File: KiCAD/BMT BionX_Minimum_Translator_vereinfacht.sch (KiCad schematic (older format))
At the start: 35 parts, among them J1 Kunteng Display Connector, J2 SAE Power Connector Motor, J3 Rosenberg Motor, J4 External BB Torquesensor, J5 Brake connector, J6 Throttle connector, J7 CAN Connector, J9 Batterieanschluß, Q1 IRF3205, Q2 IRF3205, Q3 BCP56, U1 BP, U2 MCP2551-CAN Transceiver, U3 VOM1271, U4 SD12-5, U5 VOM1271

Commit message: Schematic as PDF
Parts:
- added C7, C8, C9: 10µ, Capacitor_THT:CP_Radial_D5.0mm_P2.50mm, symbol Device:CP
- added U6: LM7812_TO220, Package_TO_SOT_THT:TO-220-3_Vertical, symbol Regulator_Linear:LM7812_TO220
- added U7: LM7805_TO220, Package_TO_SOT_THT:TO-220-3_Vertical, symbol Regulator_Linear:LM7805_TO220
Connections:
- net GND: now also C7.2, C8.2, C9.2, U6.2 (GND), U7.2 (GND)
- net at J3.1 (Pin_1), J4.1 (Pin_1), U4.+12V: now also C8.1, U6.3 (VO), U7.1 (VI)
- net at J5.1 (Pin_1), J6.1 (Pin_1), U1.5V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: now also C9.1, U7.3 (VO)
- net at R12.2, U4.V_in: now also C7.1, U6.1 (VI)
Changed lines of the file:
@@
 $EndComp
 Wire Wire Line
-	5650 2450 5650 2550
+	5650 2450 5650 2500
 $Comp
 L Device:R R11
@@
 Wire Wire Line
 	4950 2750 4950 2550
+$Comp
+L Regulator_Linear:LM7812_TO220 U6
+U 1 1 5F87B01F
+P 2450 4950
+F 0 "U6" H 2450 5192 50  0000 C CNN
+F 1 "LM7812_TO220" H 2450 5101 50  0000 C CNN
+F 2 "Package_TO_SOT_THT:TO-220-3_Vertical" H 2450 5175 50  0001 C CIN
+F 3 "http://www.fairchildsemi.com/ds/LM/LM7805.pdf" H 2450 4900 50  0001 C CNN
+	1    2450 4950
+	1    0    0    -1
+$EndComp
+$Comp
+L Regulator_Linear:LM7805_TO220 U7
+U 1 1 5F87C4AD
+P 2450 5650
+F 0 "U7" H 2450 5892 50  0000 C CNN
+F 1 "LM7805_TO220" H 2450 5801 50  0000 C CNN
+F 2 "Package_TO_SOT_THT:TO-220-3_Vertical" H 2450 5875 50  0001 C CIN
+F 3 "http://www.fairchildsemi.com/ds/LM/LM7805.pdf" H 2450 5600 50  0001 C CNN
+	1    2450 5650
+	1    0    0    -1
+$EndComp
+$Comp
+L Device:CP C8
+U 1 1 5F87D97A
+P 3000 5050
+F 0 "C8" H 3118 5096 50  0000 L CNN
+F 1 "10µ" H 3118 5005 50  0000 L CNN
+F 2 "Capacitor_THT:CP_Radial_D5.0mm_P2.50mm" H 3038 4900 50  0001 C CNN
+F 3 "~" H 3000 5050 50  0001 C CNN
+	1    3000 5050
+	1    0    0    -1
+$EndComp
+$Comp
+L Device:CP C7
+U 1 1 5F87E84B
+P 1700 5050
+F 0 "C7" H 1818 5096 50  0000 L CNN
+F 1 "10µ" H 1818 5005 50  0000 L CNN
+F 2 "Capacitor_THT:CP_Radial_D5.0mm_P2.50mm" H 1738 4900 50  0001 C CNN
+F 3 "~" H 1700 5050 50  0001 C CNN
+	1    1700 5050
+	1    0    0    -1
+$EndComp
+$Comp
+L Device:CP C9
+U 1 1 5F87F419
+P 3050 5700
+F 0 "C9" H 3168 5746 50  0000 L CNN
+F 1 "10µ" H 3168 5655 50  0000 L CNN
+F 2 "Capacitor_THT:CP_Radial_D5.0mm_P2.50mm" H 3088 5550 50  0001 C CNN
+F 3 "~" H 3050 5700 50  0001 C CNN
+	1    3050 5700
+	1    0    0    -1
+$EndComp
+Wire Wire Line
+	1300 4350 1300 5250
+Wire Wire Line
+	1300 5250 1700 5250
+Connection ~ 1300 4350
+Wire Wire Line
+	2450 5250 3000 5250
+Wire Wire Line
+	3000 5250 3000 5200
+Connection ~ 2450 5250
+Wire Wire Line
+	1700 5250 1700 5200
+Connection ~ 1700 5250
+Wire Wire Line
+	1700 5250 2450 5250
+Wire Wire Line
+	1300 5250 1300 5950
+Wire Wire Line
+	1300 5950 2450 5950
+Connection ~ 1300 5250
+Wire Wire Line
+	2450 5950 3050 5950
+Wire Wire Line
+	3050 5850 3050 5950
+Connection ~ 2450 5950
+Wire Wire Line
+	4900 4300 4150 4300
+Wire Wire Line
+	4150 4300 4150 5450
+Wire Wire Line
+	4150 5450 3050 5450
+Wire Wire Line
+	2750 5450 2750 5650
+Connection ~ 4900 4300
+Wire Wire Line
+	3050 5450 3050 5550
+Connection ~ 3050 5450
+Wire Wire Line
+	3050 5450 2750 5450
+Wire Wire Line
+	5500 4100 3850 4100
+Wire Wire Line
+	3850 4100 3850 4900
+Wire Wire Line
+	3850 4900 3450 4900
+Connection ~ 5500 4100
+Wire Wire Line
+	2750 4900 2750 4950
+Wire Wire Line
+	3000 4900 2750 4900
+Connection ~ 3000 4900
+Wire Wire Line
+	5650 2500 5350 2500
+Wire Wire Line
+	5350 2500 5350 2750
+Wire Wire Line
+	5350 2750 5050 2750
+Wire Wire Line
+	5050 2750 5050 3850
+Wire Wire Line
+	5050 3850 3450 3850
+Wire Wire Line
+	3450 3850 3450 4600
+Wire Wire Line
+	3450 4600 2050 4600
+Wire Wire Line
+	2050 4600 2050 4900
+Wire Wire Line
+	2050 4950 2150 4950
+Connection ~ 5650 2500
+Wire Wire Line
+	5650 2500 5650 2550
+Wire Wire Line
+	2050 4900 1700 4900
+Connection ~ 2050 4900
+Wire Wire Line
+	2050 4900 2050 4950
+Wire Wire Line
+	3450 4900 3450 5350
+Wire Wire Line
+	3450 5350 2000 5350
+Wire Wire Line
+	2000 5350 2000 5650
+Wire Wire Line
+	2000 5650 2150 5650
+Connection ~ 3450 4900
+Wire Wire Line
+	3450 4900 3000 4900
 $EndSCHEMATC

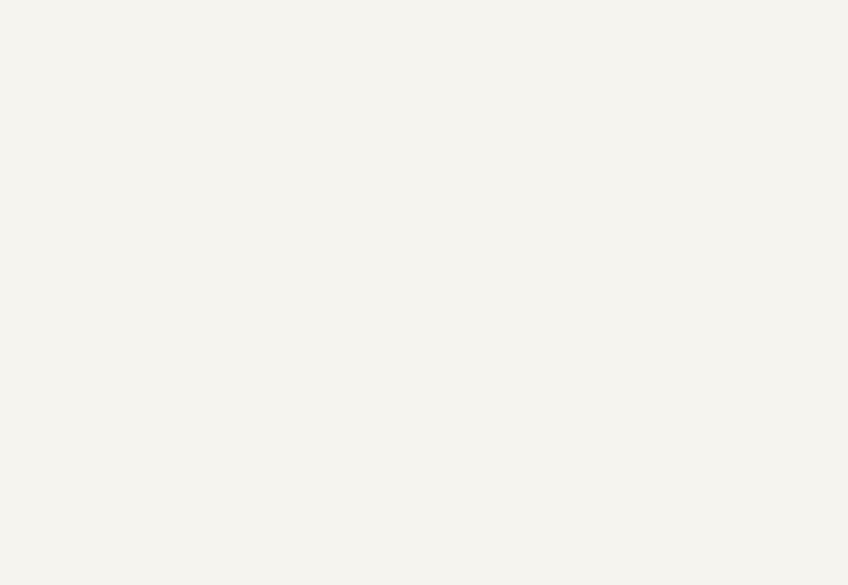
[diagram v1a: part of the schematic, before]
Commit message: added filter for speedsignal
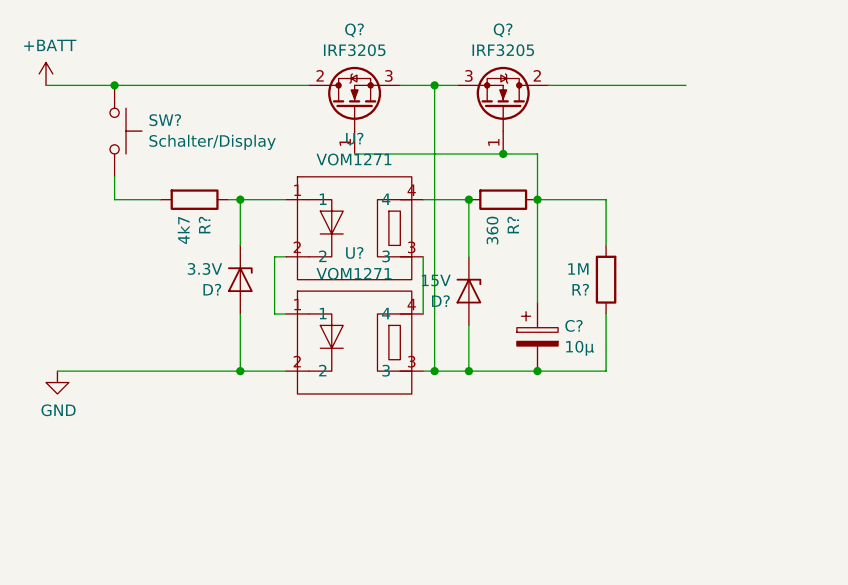
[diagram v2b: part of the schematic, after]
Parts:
- added C?: 10µ, Capacitor_THT:CP_Radial_D5.0mm_P2.50mm, symbol Device:CP
- added D?: 15V, Diode_SMD:D_0805_2012Metric, symbol Device:D_Zener
- added D?: 3.3V, Diode_SMD:D_0805_2012Metric, symbol Device:D_Zener
- added Q? (x2): IRF3205, Package_TO_SOT_THT:TO-220-3_Vertical, symbol Transistor_FET:IRF3205
- added R?: 360, Resistor_SMD:R_0805_2012Metric, symbol Device:R
- added R?: 4k7, Resistor_SMD:R_0805_2012Metric, symbol Device:R
- added R?: 1M, Resistor_SMD:R_0805_2012Metric, symbol Device:R
- added SW?: Schalter/Display, symbol Switch:SW_Push
- added U? (x2): VOM1271, Package_SO:SOP-4_3.8x4.1mm_P2.54mm, symbol Driver_FET:VOM1271
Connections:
- net +BATT: now also Q?.2 (D), SW?.1
- net GND: now also D?.2 (A), U?.2
- new net: C?.1, Q?.1 (G), Q?.1 (G), R?.1, R?.2
- new net: C?.2, D?.2 (A), Q?.3 (S), Q?.3 (S), R?.1, U?.3
- new net: D?.1 (K), R?.1, U?.1
- new net: U?.1, U?.2
- new net: U?.3, U?.4
- new net: D?.1 (K), R?.2, U?.4
- new net: R?.2, SW?.2
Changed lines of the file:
@@
 Wire Wire Line
 	3450 4900 3000 4900
+$Comp
+L Transistor_FET:IRF3205 Q?
+U 1 1 5FA7240E
+P -2000 750
+F 0 "Q?" V -1657 750 50  0000 C CNN
+F 1 "IRF3205" V -1748 750 50  0000 C CNN
+F 2 "Package_TO_SOT_THT:TO-220-3_Vertical" H -1750 675 50  0001 L CIN
+F 3 "http://www.irf.com/product-info/datasheets/data/irf3205.pdf" H -2000 750 50  0001 L CNN
+	1    -2000 750
+	0    -1   -1   0
+$EndComp
+$Comp
+L Transistor_FET:IRF3205 Q?
+U 1 1 5FA72414
+P -1350 750
+F 0 "Q?" V -1007 750 50  0000 C CNN
+F 1 "IRF3205" V -1098 750 50  0000 C CNN
+F 2 "Package_TO_SOT_THT:TO-220-3_Vertical" H -1100 675 50  0001 L CIN
+F 3 "http://www.irf.com/product-info/datasheets/data/irf3205.pdf" H -1350 750 50  0001 L CNN
+	1    -1350 750
+	0    1    -1   0
+$EndComp
+$Comp
+L Driver_FET:VOM1271 U?
+U 1 1 5FA7241A
+P -2000 900
+F 0 "U?" H -2000 915 50  0000 C CNN
+F 1 "VOM1271" H -2000 824 50  0000 C CNN
+F 2 "Package_SO:SOP-4_3.8x4.1mm_P2.54mm" H -2000 900 50  0001 C CNN
+F 3 "" H -2000 900 50  0001 C CNN
+	1    -2000 900
+	1    0    0    -1
+$EndComp
+$Comp
+L Driver_FET:VOM1271 U?
+U 1 1 5FA72420
+P -2000 1400
+F 0 "U?" H -2000 1415 50  0000 C CNN
+F 1 "VOM1271" H -2000 1324 50  0000 C CNN
+F 2 "Package_SO:SOP-4_3.8x4.1mm_P2.54mm" H -2000 1400 50  0001 C CNN
+F 3 "" H -2000 1400 50  0001 C CNN
+	1    -2000 1400
+	1    0    0    -1
+$EndComp
+Wire Wire Line
+	-2350 1650 -2300 1650
+Wire Wire Line
+	-1700 1650 -1700 1400
+Wire Wire Line
+	-1700 1150 -1500 1150
+Wire Wire Line
+	-1700 1900 -1650 1900
+Wire Wire Line
+	-1650 1900 -1650 650
+Connection ~ -1650 650
+Wire Wire Line
+	-1650 650  -1550 650
+$Comp
+L Device:D_Zener D?
+U 1 1 5FA7243B
+P -1500 1550
+F 0 "D?" V -1454 1471 50  0000 R CNN
+F 1 "15V" V -1545 1471 50  0000 R CNN
+F 2 "Diode_SMD:D_0805_2012Metric" H -1500 1550 50  0001 C CNN
+F 3 "~" H -1500 1550 50  0001 C CNN
+	1    -1500 1550
+	0    1    1    0
+$EndComp
+Wire Wire Line
+	-3350 650  -3050 650
+Wire Wire Line
+	-2300 1400 -2350 1400
+Wire Wire Line
+	-2350 1400 -2350 1650
+$Comp
+L Device:R R?
+U 1 1 5FAA2E19
+P -1350 1150
+F 0 "R?" H -1280 1196 50  0000 L CNN
+F 1 "360" H -1280 1105 50  0000 L CNN
+F 2 "Resistor_SMD:R_0805_2012Metric" V -1420 1150 50  0001 C CNN
+F 3 "~" H -1350 1150 50  0001 C CNN
+	1    -1350 1150
+	0    1    1    0
+$EndComp
+Wire Wire Line
+	-1500 1150 -1500 1400
+Wire Wire Line
+	-1800 650  -1650 650
+Wire Wire Line
+	-2000 950  -1350 950
+Connection ~ -1500 1150
+Wire Wire Line
+	-1500 1700 -1500 1900
+Wire Wire Line
+	-1500 1900 -1650 1900
+Connection ~ -1650 1900
+$Comp
+L Device:CP C?
+U 1 1 5FAE6A47
+P -1200 1750
+F 0 "C?" H -1082 1796 50  0000 L CNN
+F 1 "10µ" H -1082 1705 50  0000 L CNN
+F 2 "Capacitor_THT:CP_Radial_D5.0mm_P2.50mm" H -1162 1600 50  0001 C CNN
+F 3 "~" H -1200 1750 50  0001 C CNN
+	1    -1200 1750
+	1    0    0    -1
+$EndComp
+Wire Wire Line
+	-1500 1900 -1200 1900
+Connection ~ -1500 1900
+Wire Wire Line
+	-1200 1600 -1200 1150
+Wire Wire Line
+	-1200 1150 -1200 950
+Wire Wire Line
+	-1200 950  -1350 950
+Connection ~ -1200 1150
+Connection ~ -1350 950
+$Comp
+L Device:D_Zener D?
+U 1 1 5FB2B7AF
+P -2500 1500
+F 0 "D?" V -2454 1421 50  0000 R CNN
+F 1 "3.3V" V -2545 1421 50  0000 R CNN
+F 2 "Diode_SMD:D_0805_2012Metric" H -2500 1500 50  0001 C CNN
+F 3 "~" H -2500 1500 50  0001 C CNN
+	1    -2500 1500
+	0    1    1    0
+$EndComp
+$Comp
+L Switch:SW_Push SW?
+U 1 1 5FB2D20E
+P -3050 850
+F 0 "SW?" V -3096 998 50  0000 L CNN
+F 1 "Schalter/Display" V -3005 998 50  0000 L CNN
+F 2 "" H -3050 1050 50  0001 C CNN
+F 3 "~" H -3050 1050 50  0001 C CNN
+	1    -3050 850
+	0    1    1    0
+$EndComp
+Connection ~ -3050 650
+Wire Wire Line
+	-3050 650  -2200 650
+$Comp
+L Device:R R?
+U 1 1 5FB45B50
+P -2700 1150
+F 0 "R?" H -2630 1196 50  0000 L CNN
+F 1 "4k7" H -2630 1105 50  0000 L CNN
+F 2 "Resistor_SMD:R_0805_2012Metric" V -2770 1150 50  0001 C CNN
+F 3 "~" H -2700 1150 50  0001 C CNN
+	1    -2700 1150
+	0    1    1    0
+$EndComp
+Wire Wire Line
+	-3050 1050 -3050 1150
+Wire Wire Line
+	-3050 1150 -2850 1150
+Wire Wire Line
+	-2550 1150 -2500 1150
+Wire Wire Line
+	-2500 1150 -2500 1350
+Connection ~ -2500 1150
+Wire Wire Line
+	-2500 1150 -2300 1150
+Wire Wire Line
+	-2500 1650 -2500 1900
+Wire Wire Line
+	-2500 1900 -2300 1900
+$Comp
+L power:+BATT #PWR?
+U 1 1 5FBA561B
+P -3350 650
+F 0 "#PWR?" H -3350 500 50  0001 C CNN
+F 1 "+BATT" H -3335 823 50  0000 C CNN
+F 2 "" H -3350 650 50  0001 C CNN
+F 3 "" H -3350 650 50  0001 C CNN
+	1    -3350 650
+	1    0    0    -1
+$EndComp
+$Comp
+L power:GND #PWR?
+U 1 1 5FBA62CD
+P -3300 1900
+F 0 "#PWR?" H -3300 1650 50  0001 C CNN
+F 1 "GND" H -3295 1727 50  0000 C CNN
+F 2 "" H -3300 1900 50  0001 C CNN
+F 3 "" H -3300 1900 50  0001 C CNN
+	1    -3300 1900
+	1    0    0    -1
+$EndComp
+Wire Wire Line
+	-3300 1900 -2500 1900
+Connection ~ -2500 1900
+Wire Wire Line
+	-1150 650  -550 650
+$Comp
+L Device:R R?
+U 1 1 5FBD75F6
+P -900 1500
+F 0 "R?" H -830 1546 50  0000 L CNN
+F 1 "1M" H -830 1455 50  0000 L CNN
+F 2 "Resistor_SMD:R_0805_2012Metric" V -970 1500 50  0001 C CNN
+F 3 "~" H -900 1500 50  0001 C CNN
+	1    -900 1500
+	-1   0    0    1
+$EndComp
+Wire Wire Line
+	-1200 1150 -900 1150
+Wire Wire Line
+	-900 1150 -900 1350
+Wire Wire Line
+	-900 1650 -900 1900
+Wire Wire Line
+	-900 1900 -1200 1900
+Connection ~ -1200 1900
 $EndSCHEMATC
